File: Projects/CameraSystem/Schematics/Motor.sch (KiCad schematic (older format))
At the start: 3 parts

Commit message: feat: schematic updated
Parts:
- gave numbers to parts that had none: 3
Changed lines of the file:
@@
 	1400 1250 1550 1250
 $Comp
-L Connector_Generic:Conn_02x02_Odd_Even J?
+L Connector_Generic:Conn_02x02_Odd_Even J13
 U 1 1 5BC62F82
 P 1800 1200
-F 0 "J?" H 1850 1417 50  0000 C CNN
+F 0 "J13" H 1850 1417 50  0000 C CNN
 F 1 "Conn_02x02_Odd_Even" H 1850 1326 50  0000 C CNN
 F 2 "" H 1800 1200 50  0001 C CNN
@@
 	3650 1450 3850 1450
 $Comp
-L Connector_Generic:Conn_02x05_Counter_Clockwise J?
+L Connector_Generic:Conn_02x05_Counter_Clockwise J15
 U 1 1 5BC641C3
 P 3350 1450
-F 0 "J?" H 3400 1867 50  0000 C CNN
+F 0 "J15" H 3400 1867 50  0000 C CNN
 F 1 "Conn_02x05_Counter_Clockwise" H 3400 1776 50  0000 C CNN
 F 2 "" H 3350 1450 50  0001 C CNN
@@
 $EndComp
 $Comp
-L Connector_Generic:Conn_02x05_Counter_Clockwise J?
+L Connector_Generic:Conn_02x05_Counter_Clockwise J14
 U 1 1 5BC64226
 P 1800 2400
-F 0 "J?" H 1850 2817 50  0000 C CNN
+F 0 "J14" H 1850 2817 50  0000 C CNN
 F 1 "Conn_02x05_Counter_Clockwise" H 1850 2726 50  0000 C CNN
 F 2 "" H 1800 2400 50  0001 C CNN
@@
 	3850 1350 3850 1250
 $Comp
-L power:GND #PWR?
+L power:GND #PWR0142
 U 1 1 5BC64498
 P 4600 1350
-F 0 "#PWR?" H 4600 1100 50  0001 C CNN
+F 0 "#PWR0142" H 4600 1100 50  0001 C CNN
 F 1 "GND" H 4605 1177 50  0000 C CNN
 F 2 "" H 4600 1350 50  0001 C CNN

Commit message: feat: symbol assignment updated
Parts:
- removed J14: Conn_02x05_Counter_Clockwise, symbol Connector_Generic:Conn_02x05_Counter_Clockwise
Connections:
- net labels removed: M_DIR, M_EN, M_GND, M_PWM, SENSOR1, SENSOR2, VDD_3V3
- wire segments 36 -> 23
- no-connect marks 0 -> 1
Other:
- note removed: "Use a cable with a bigger cross section for the power supply"
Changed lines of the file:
@@
-	1    0    0    -1
-$EndComp
-$Comp
-L Connector_Generic:Conn_02x05_Counter_Clockwise J14
-U 1 1 5BC64226
-P 1800 2400
-F 0 "J14" H 1850 2817 50  0000 C CNN
-F 1 "Conn_02x05_Counter_Clockwise" H 1850 2726 50  0000 C CNN
-F 2 "" H 1800 2400 50  0001 C CNN
-F 3 "~" H 1800 2400 50  0001 C CNN
-	1    1800 2400
 	1    0    0    -1
 $EndComp
@@
 Text HLabel 3850 1550 2    50   Output ~ 0
 SENSOR2_CON
-Wire Wire Line
-	1600 2200 1250 2200
-Wire Wire Line
-	1250 2200 1250 2300
-Wire Wire Line
-	1250 2300 1600 2300
-Connection ~ 1250 2200
-Wire Wire Line
-	1250 2200 1050 2200
-Wire Wire Line
-	2450 2200 2450 2300
-Wire Wire Line
-	2450 2200 2650 2200
-Connection ~ 2450 2200
-Text Label 1050 2200 0    50   ~ 0
-VDD_3V3
-Text Label 2650 2200 2    50   ~ 0
-M_GND
-Wire Wire Line
-	1600 2400 1250 2400
-Wire Wire Line
-	1600 2500 1250 2500
-Wire Wire Line
-	1600 2600 1250 2600
-Text Label 2650 2400 2    50   ~ 0
-SENSOR1
-Text Label 2650 2500 2    50   ~ 0
-SENSOR2
-Text Label 1250 2600 0    50   ~ 0
-M_EN
-Text Label 1250 2500 0    50   ~ 0
-M_DIR
-Text Label 1250 2400 0    50   ~ 0
-M_PWM
-Wire Wire Line
-	2100 2300 2450 2300
-Wire Wire Line
-	2100 2200 2450 2200
-Wire Wire Line
-	2100 2400 2650 2400
-Wire Wire Line
-	2100 2500 2650 2500
-Text Notes 850  1900 0    50   ~ 0
-Use a cable with a bigger cross section for the power supply
+NoConn ~ 3650 1650
 $EndSCHEMATC

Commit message: feat: assign footprints
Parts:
- removed J15: Conn_02x05_Counter_Clockwise, symbol Connector_Generic:Conn_02x05_Counter_Clockwise
- added J14: Conn_02x05_Odd_Even, Pin_Headers:Pin_Header_Straight_2x05_Pitch2.54mm, symbol Connector_Generic:Conn_02x05_Odd_Even
- J13: footprint (none) -> Pin_Headers:Pin_Header_Straight_2x02_Pitch2.54mm_SMD
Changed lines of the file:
@@
 F 0 "J13" H 1850 1417 50  0000 C CNN
 F 1 "Conn_02x02_Odd_Even" H 1850 1326 50  0000 C CNN
-F 2 "" H 1800 1200 50  0001 C CNN
+F 2 "Pin_Headers:Pin_Header_Straight_2x02_Pitch2.54mm_SMD" H 1800 1200 50  0001 C CNN
 F 3 "~" H 1800 1200 50  0001 C CNN
 	1    1800 1200
@@
 Wire Wire Line
 	3650 1450 3850 1450
-$Comp
-L Connector_Generic:Conn_02x05_Counter_Clockwise J15
-U 1 1 5BC641C3
-P 3350 1450
-F 0 "J15" H 3400 1867 50  0000 C CNN
-F 1 "Conn_02x05_Counter_Clockwise" H 3400 1776 50  0000 C CNN
-F 2 "" H 3350 1450 50  0001 C CNN
-F 3 "~" H 3350 1450 50  0001 C CNN
-	1    3350 1450
-	1    0    0    -1
-$EndComp
 Wire Wire Line
 	2900 1250 2900 1350
@@
 SENSOR2_CON
 NoConn ~ 3650 1650
+$Comp
+L Connector_Generic:Conn_02x05_Odd_Even J14
+U 1 1 5BC2EB0E
+P 3350 1450
+F 0 "J14" H 3400 1867 50  0000 C CNN
+F 1 "Conn_02x05_Odd_Even" H 3400 1776 50  0000 C CNN
+F 2 "Pin_Headers:Pin_Header_Straight_2x05_Pitch2.54mm" H 3350 1450 50  0001 C CNN
+F 3 "~" H 3350 1450 50  0001 C CNN
+	1    3350 1450
+	1    0    0    -1
+$EndComp
 $EndSCHEMATC

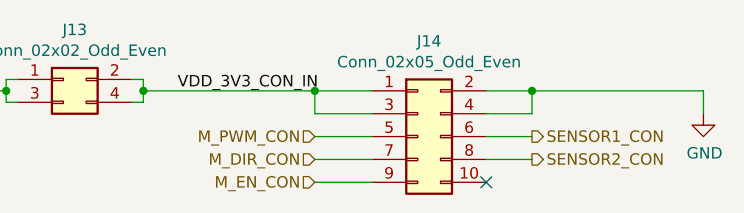
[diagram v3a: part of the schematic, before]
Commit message: feat: routing first draft finished
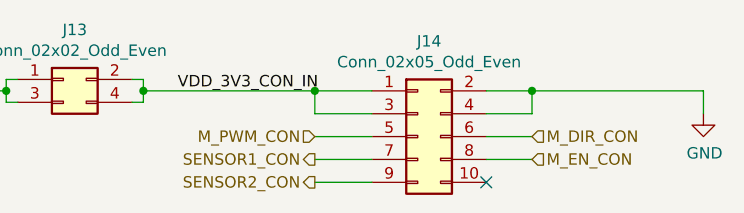
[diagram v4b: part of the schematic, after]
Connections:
- net M_DIR_CON: now also J14.6 (Pin_6); no longer J14.7 (Pin_7)
- net M_EN_CON: now also J14.8 (Pin_8); no longer J14.9 (Pin_9)
- net SENSOR1_CON: now also J14.7 (Pin_7); no longer J14.6 (Pin_6)
- net SENSOR2_CON: now also J14.9 (Pin_9); no longer J14.8 (Pin_8)
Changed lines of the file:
@@
 $Descr A4 11693 8268
 encoding utf-8
-Sheet 9 9
+Sheet 8 9
 Title ""
 Date ""
@@
 	3150 1350 2900 1350
 Wire Wire Line
-	3150 1450 2900 1450
-Wire Wire Line
-	3150 1550 2900 1550
-Wire Wire Line
 	3650 1250 3850 1250
 Wire Wire Line
 	3650 1350 3850 1350
-Wire Wire Line
-	3650 1450 3850 1450
 Wire Wire Line
 	2900 1250 2900 1350
@@
 	4600 1250 4600 1350
 Connection ~ 3850 1250
-Wire Wire Line
-	3150 1650 2900 1650
-Wire Wire Line
-	3650 1550 3850 1550
 Text HLabel 2900 1450 0    50   Input ~ 0
 M_PWM_CON
-Text HLabel 2900 1550 0    50   Input ~ 0
+Text HLabel 3850 1450 2    50   Input ~ 0
 M_DIR_CON
-Text HLabel 2900 1650 0    50   Input ~ 0
+Text HLabel 3850 1550 2    50   Input ~ 0
 M_EN_CON
-Text HLabel 3850 1450 2    50   Output ~ 0
+Text HLabel 2900 1550 0    50   Output ~ 0
 SENSOR1_CON
-Text HLabel 3850 1550 2    50   Output ~ 0
+Text HLabel 2900 1650 0    50   Output ~ 0
 SENSOR2_CON
 NoConn ~ 3650 1650
@@
 	1    0    0    -1
 $EndComp
+Wire Wire Line
+	2900 1650 3150 1650
+Wire Wire Line
+	3650 1450 3850 1450
+Wire Wire Line
+	2900 1450 3150 1450
+Wire Wire Line
+	3850 1550 3650 1550
+Wire Wire Line
+	3150 1550 2900 1550
 $EndSCHEMATC

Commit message: circuit updated
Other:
- note added: "ADD IC drv8834 and switches"
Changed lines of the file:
@@
 	2100 1300 2150 1300
 Wire Wire Line
-	2150 1300 2150 1250
-Wire Wire Line
 	2150 1200 2100 1200
-Connection ~ 2150 1250
-Wire Wire Line
-	2150 1250 2150 1200
 Text Label 2300 1250 0    50   ~ 0
 VDD_3V3_CON_IN
@@
 Wire Wire Line
 	3150 1550 2900 1550
+Connection ~ 2150 1250
+Wire Wire Line
+	2150 1250 2150 1200
+Wire Wire Line
+	2150 1300 2150 1250
+Text Notes 1800 2100 0    50   ~ 0
+ADD IC drv8834 and switches
 $EndSCHEMATC

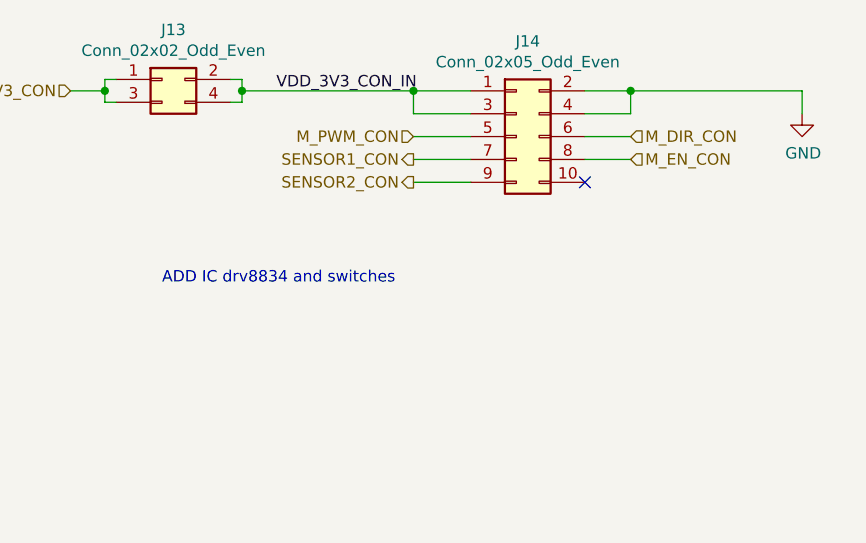
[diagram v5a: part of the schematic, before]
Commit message: change circuit
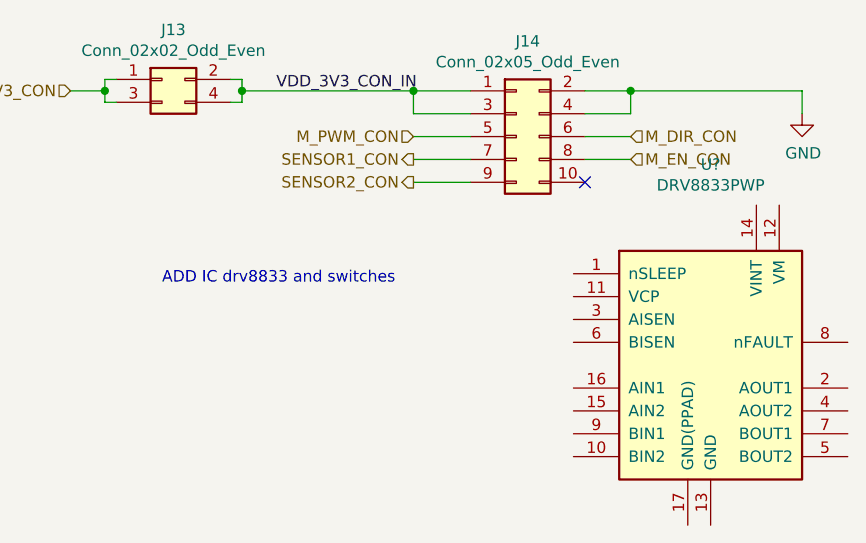
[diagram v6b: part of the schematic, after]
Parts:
- added U?: DRV8833PWP, Package_SO:HTSSOP-16-1EP_4.4x5mm_P0.65mm_EP3.4x5mm_Mask2.46x2.31mm_ThermalVias, symbol Driver_Motor:DRV8833PWP
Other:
- note added: "ADD IC drv8833 and switches"
- note removed: "ADD IC drv8834 and switches"
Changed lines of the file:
@@
 	2150 1300 2150 1250
 Text Notes 1800 2100 0    50   ~ 0
-ADD IC drv8834 and switches
+ADD IC drv8833 and switches
+$Comp
+L Driver_Motor:DRV8833PWP U?
+U 1 1 5CA61180
+P 4200 2450
+F 0 "U?" H 4200 3328 50  0000 C CNN
+F 1 "DRV8833PWP" H 4200 3237 50  0000 C CNN
+F 2 "Package_SO:HTSSOP-16-1EP_4.4x5mm_P0.65mm_EP3.4x5mm_Mask2.46x2.31mm_ThermalVias" H 4650 2900 50  0001 L CNN
+F 3 "http://www.ti.com/lit/ds/symlink/drv8833.pdf" H 4050 3000 50  0001 C CNN
+	1    4200 2450
+	1    0    0    -1
+$EndComp
 $EndSCHEMATC

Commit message: schematic updated
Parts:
- added C?: 10u, symbol Device:C
- added C?: 10n, symbol Device:C
- added C?: 2u2, symbol Device:C
- added R? (x2): 10k, symbol Device:R
- added R?: 1, symbol Device:R
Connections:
- net GND: now also U?.13 (GND), U?.17 (GND(PPAD)), C?.1, C?.2, R?.2
- net SENSOR1_CON: now also R?.1
- net SENSOR2_CON: now also R?.1
- net VDD_3V3_CON_IN: now also U?.12 (VM), C?.1, C?.2, R?.2, R?.2
- net M_NSLEEP: now reaches U?.1 (nSLEEP)
- net M_PWM_IN_2: now reaches U?.10 (BIN2)
- net M_PWM_IN_2: now also U?.15 (AIN2)
- net at U?.11 (VCP): now also C?.1
- net at U?.14 (VINT): now also C?.2
- net M_PWM_IN_1: now reaches U?.16 (AIN1)
- net M_PWM_IN_1: now also U?.9 (BIN1)
- net M_PWM_OUT_1: now reaches U?.2 (AOUT1)
- net M_PWM_OUT_1: now also U?.7 (BOUT1)
- net at U?.3 (AISEN): now also U?.6 (BISEN), R?.1
- net M_PWM_OUT_2: now reaches U?.4 (AOUT2)
- net M_PWM_OUT_2: now also U?.5 (BOUT2)
- net M_PWM_CON: no longer names the net of J14.5 (Pin_5)
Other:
- moved on the sheet: U?

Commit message: update circuit
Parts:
- removed J14: Conn_02x05_Odd_Even, Pin_Headers:Pin_Header_Straight_2x05_Pitch2.54mm, symbol Connector_Generic:Conn_02x05_Odd_Even
- removed R? (x2): 10k, symbol Device:R
- added D? (x2): LED, LED_SMD:LED_1206_3216Metric, symbol Device:LED
- added J?: Conn_02x03_Odd_Even, symbol Connector_Generic:Conn_02x03_Odd_Even
- added Q?: BC856, Package_TO_SOT_SMD:SOT-23, symbol Transistor_BJT:BC856
- added R? (x4): 10k, symbol Device:R
- added R? (x2): 560, digikey-footprints:0603, symbol Device:R
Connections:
- net GND: now also D?.1 (K), D?.1 (K)
- net M_PWM_OUT_1: now also J?.1 (Pin_1), J?.2 (Pin_2)
- net M_PWM_OUT_2: now also J?.3 (Pin_3), J?.4 (Pin_4)
- net SENSOR1_CON: now also J?.5 (Pin_5), R?.1
- net SENSOR2_CON: now also J?.6 (Pin_6), R?.1
- net VDD_3V3_CON_IN: now also Q?.2 (E), R?.2, R?.2, R?.2
- net at U?.8 (nFAULT): now also R?.1, R?.2
- new net: Q?.1 (B), R?.1, R?.1
- new net: Q?.3 (C), R?.1
- new net: D?.2 (A), R?.2 (x2)
- no-connect marks 1 -> 0
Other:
- moved on the sheet: C?, J13, R?, U?
